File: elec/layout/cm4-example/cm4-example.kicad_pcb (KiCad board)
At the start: 4 copper layers, 109 parts, among them U10 10kΩ ±1% 62.5mW, U11 10kΩ ±1% 62.5mW, U13 1kΩ ±1% 62.5mW, U14 1kΩ ±1% 62.5mW, U15 100nF ±10% 16V X7R, U16 10kΩ ±1% 62.5mW, U17 10kΩ ±1% 62.5mW, U19 100nF ±10% 16V X7R, U2 1µF ±10% 25V X5R, U20 10kΩ ±1% 62.5mW, U21 10kΩ ±1% 62.5mW, U22 1kΩ ±1% 62.5mW, U23 1kΩ ±1% 62.5mW, U24 1µF ±10% 25V X5R, U26 1µF ±10% 25V X5R, U27 4.7µF ±10% 10V X5R, U28 10µF ±10% 10V X5R, U3 10kΩ ±1% 62.5mW, U31 1µF ±10% 25V X5R, U33 10pF ±5% 50V C0G, U34 10pF ±5% 50V C0G, U35 4.7µF ±10% 10V X5R, U36 10µF ±10% 10V X5R, U38 4.7nF ±10% 50V X7R, U39 60.4Ω ±1% 100mW, U4 10kΩ ±1% 62.5mW, U40 60.4Ω ±1% 100mW, U41 1µF ±10% 25V X5R, U42 1µF ±10% 25V X5R, U45 100nF ±10% 16V X7R, U46 2.2µF ±10% 25V X5R, U48 10kΩ ±1% 62.5mW, U49 10kΩ ±1% 62.5mW, U50 10kΩ ±1% 62.5mW, U51 10kΩ ±1% 62.5mW, U52 10kΩ ±1% 62.5mW, U53 10kΩ ±1% 62.5mW, U54 10kΩ ±1% 62.5mW, U55 10kΩ ±1% 62.5mW, U56 10kΩ ±1% 62.5mW, U57 10kΩ ±1% 62.5mW, U58 10kΩ ±1% 62.5mW, U59 10kΩ ±1% 62.5mW, U6 1kΩ ±1% 62.5mW, U60 10kΩ ±1% 62.5mW, U61 10kΩ ±1% 62.5mW, U62 10kΩ ±1% 62.5mW, U63 10kΩ ±1% 62.5mW, U64 10kΩ ±1% 62.5mW, U65 1kΩ ±1% 62.5mW, U66 1kΩ ±1% 62.5mW, U67 1µF ±10% 25V X5R, U69 1µF ±10% 25V X5R, U7 1kΩ ±1% 62.5mW, U70 470nF ±20% 16V X5R, U71 1kΩ ±1% 62.5mW, U72 1kΩ ±1% 62.5mW, U75 2.2µF ±20% 6.3V X5R, U76 10µF ±10% 25V X5R, U9 1µF ±10% 25V X5R

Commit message: initial routuing
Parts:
- moved U62 107.6 mm to (170.1, 94.9), turned to 90 degrees
- moved U45 107.4 mm to (173.1, 88.4), turned to 90 degrees
- moved U63 105.8 mm to (169.0, 94.9), turned to 90 degrees
- moved U46 104.9 mm to (171.8, 88.4), turned to 90 degrees
- moved U60 104.0 mm to (168.0, 94.9), turned to 90 degrees
- moved U61 102.3 mm to (166.9, 94.9), turned to 90 degrees
- moved U58 100.5 mm to (165.9, 94.9), turned to 90 degrees
- moved U64 99.7 mm to (171.2, 82.5), turned to 90 degrees
- moved U59 98.7 mm to (164.8, 94.9), turned to 90 degrees
- moved U49 97.7 mm to (170.1, 82.5), turned to -90 degrees
- moved U56 97.0 mm to (163.8, 94.9), turned to 90 degrees
- moved U47 95.8 mm to (166.7, 88.6), turned to 180 degrees
- moved U48 95.6 mm to (169.0, 82.5), turned to -90 degrees
- moved U57 95.3 mm to (162.8, 94.9), turned to 90 degrees
- moved U51 93.6 mm to (168.0, 82.5), turned to -90 degrees
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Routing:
- net cs: track 0.00 -> 54.9 mm, vias 0 -> 2
- net sck: track 0.00 -> 50.9 mm
- net mosi: track 0.00 -> 50.5 mm
- net miso: track 0.00 -> 45.7 mm
- net hv-3: track 47.3 -> 74.6 mm, vias 0 -> 9
- net gnd: track 66.3 -> 91.7 mm
- net io-1: track 0.00 -> 13.9 mm
- net VSINK_VCC: track 0.00 -> 13.3 mm
- net CANL: track 4.55 -> 17.4 mm
- net hv-1: track 16.7 -> 28.7 mm, vias 0 -> 2
- net VCC_5V: track 12.4 -> 22.5 mm
- net CANH: track 7.34 -> 15.2 mm
- net gnd-2: track 45.0 -> 52.2 mm
- added copper zone on F.Cu, net cathode-1
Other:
- board outline added: 100 x 100 mm

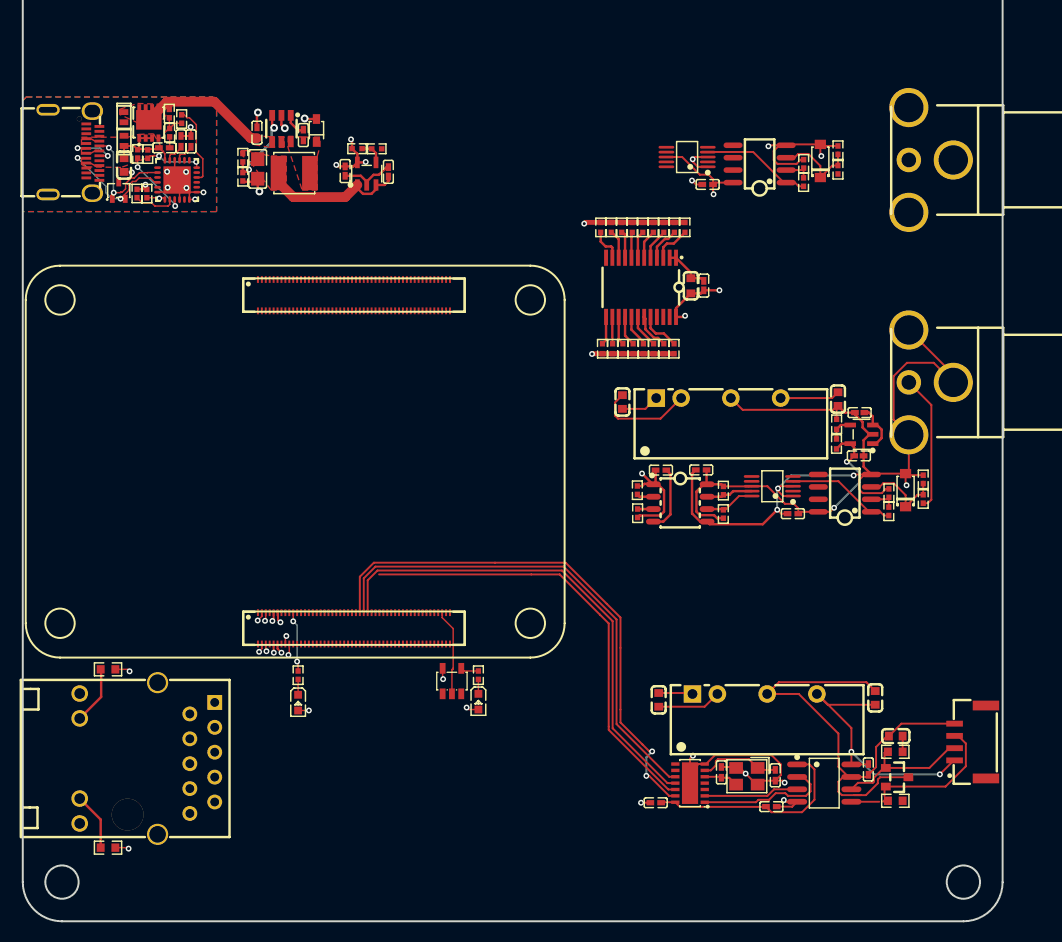
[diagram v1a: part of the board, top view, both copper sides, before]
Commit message: fixed SPI pinout
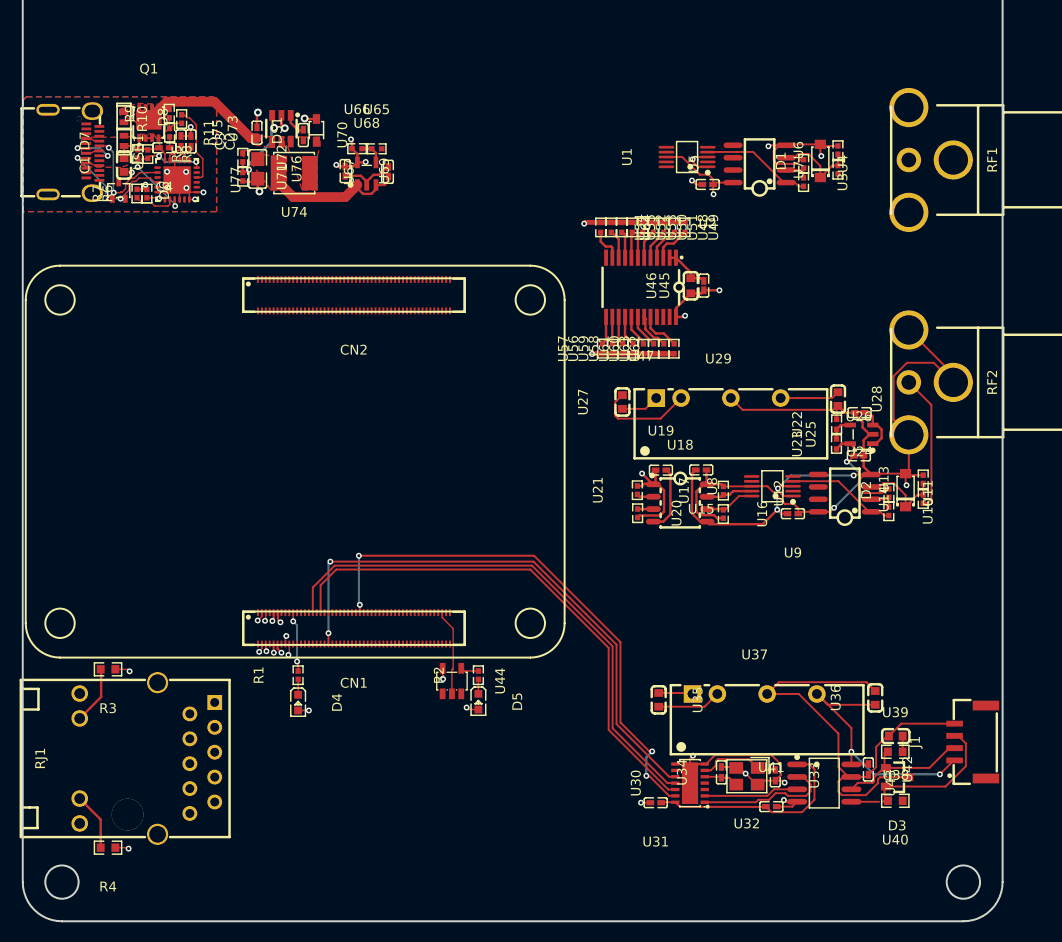
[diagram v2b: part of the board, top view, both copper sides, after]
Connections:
- net ADJ_NC renamed regulator_3v3-out
- net FB renamed regulator_5v-out
- net controller-line-2 renamed controller.cm4-pins[38]
- net out renamed analog_in_2.regulator_3v3_isolated-out
- net pins[38] renamed controller.cm4.hdi_b-pins[38]
- CN1 pad 15: controller-line-3 -> mosi
- CN1 pad 17: controller-line-1 -> miso
- CN1 pad 20: controller.cm4-line -> controller.cm4-line-1
- CN1 pad 22: controller.cm4-line-1 -> controller.cm4-line-3
- CN1 pad 28: sck -> pins[55]
- CN1 pad 29: mosi -> controller.cm4-line-2
- CN1 pad 78: controller.cm4-pins[44]-1 -> controller.cm4-pins[44]
- CN1 pad 80: controller.cm4-line-2 -> controller.cm4-line
- CN1 pad 82: controller-line -> sck
- CN2 pad 78: controller.cm4-pins[44] -> controller.cm4-pins[44]-1
- D1 pad 1: cathode -> cathode-2
- D2 pad 1: cathode-2 -> cathode-1
- D2 pad 2: gnd -> gnd-1
- D3 pad 3: gnd-2 -> gnd
- DS1 pad 1: cathode-1 -> cathode
- J1 pad 1: hv-1 -> hv-2
- J1 pad 4: gnd-2 -> gnd
- RF2 pad 2: gnd -> gnd-1
- RF2 pad 3: gnd -> gnd-1
- RF2 pad 4: gnd -> gnd-1
- RJ1 pad P1: controller.rj45.connector-net-1 -> controller.rj45.connector-net
- RJ1 pad P10: controller.rj45.connector-net -> controller.rj45.connector-net-1
- RJ1 pad SHIELD0: gnd-1 -> gnd-2
- RJ1 pad SHIELD1: gnd-1 -> gnd-2
- U1 pad 10: line -> line-3
- U1 pad 4: output -> output-1
- U1 pad 8: hv-3 -> hv
- U1 pad 9: line-2 -> line-1
- U10 pad 2: output-1 -> output
- U11 pad 1: gnd -> gnd-1
- U12 pad 1: output-1 -> output
- U12 pad 3: cathode-2 -> cathode-1
- U12 pad 4: gnd -> gnd-1
- U12 pad 8: hv-2 -> hv-3
- U13 pad 1: cathode-2 -> cathode-1
- U13 pad 2: gnd -> gnd-1
- U14 pad 2: cathode-2 -> cathode-1
- U15 pad 1: hv-2 -> hv-3
- U15 pad 2: gnd -> gnd-1
- U16 pad 2: hv-2 -> hv-3
- U17 pad 2: hv-2 -> hv-3
- U18 pad 1: hv-3 -> hv
- U18 pad 2: line-3 -> line
- U18 pad 3: line-1 -> line-2
- U18 pad 5: gnd -> gnd-1
- U18 pad 8: hv-2 -> hv-3
- U19 pad 1: hv-3 -> hv
- U2 pad 1: hv-3 -> hv
- U20 pad 1: line-1 -> line-2
- U20 pad 2: hv-3 -> hv
- U21 pad 1: line-3 -> line
- U21 pad 2: hv-3 -> hv
- U22 pad 2: gnd -> gnd-1
- U23 pad 1: hv-2 -> hv-3
- U24 pad 1: hv -> hv-1
- U24 pad 2: gnd -> gnd-1
- U25 pad 1: hv -> hv-1
- U25 pad 2: gnd -> gnd-1
- U25 pad 3: hv -> hv-1
- U25 pad 5: hv-2 -> hv-3
- U26 pad 1: hv-2 -> hv-3
- U26 pad 2: gnd -> gnd-1
- U28 pad 1: hv -> hv-1
- U28 pad 2: gnd -> gnd-1
- U29 pad 4: gnd -> gnd-1
- U29 pad 6: hv -> hv-1
- U3 pad 2: output -> output-1
- U30 pad 14: hv-3 -> hv
- U30 pad 4: can_interface.controller-io -> can_interface.controller-io-2
- U30 pad 8: can_interface.controller-io-1 -> can_interface.controller-io
- U30 pad 9: can_interface.controller-io-2 -> can_interface.controller-io-1
- U31 pad 1: hv-3 -> hv
- U36 pad 1: hv-1 -> hv-2
- U36 pad 2: gnd-2 -> gnd
- U37 pad 4: gnd-2 -> gnd
- U37 pad 6: hv-1 -> hv-2
- U38 pad 2: gnd-2 -> gnd
- U41 pad 1: hv-3 -> hv
- U42 pad 1: hv-1 -> hv-2
- U42 pad 2: gnd-2 -> gnd
- U43 pad 1: hv-3 -> hv
- U43 pad 7: gnd-2 -> gnd
- U43 pad 8: hv-1 -> hv-2
- U45 pad 1: hv-3 -> hv
- U46 pad 1: hv-3 -> hv
- U47 pad 10: i2c_multiplexer-line-1 -> i2c_multiplexer-line-8
- U47 pad 11: i2c_multiplexer-line-8 -> i2c_multiplexer-line-4
- U47 pad 13: line-3 -> line
- U47 pad 14: line-1 -> line-2
- U47 pad 15: i2c_multiplexer-line-4 -> i2c_multiplexer-line-3
- U47 pad 16: i2c_multiplexer-line-6 -> i2c_multiplexer-line-11
- U47 pad 18: i2c_multiplexer-line-5 -> i2c_multiplexer-line
- U47 pad 19: i2c_multiplexer-line-3 -> i2c_multiplexer-line-1
- U47 pad 20: i2c_multiplexer-line-7 -> i2c_multiplexer-line-10
- U47 pad 24: hv-3 -> hv
- U47 pad 4: line-2 -> line-1
- U47 pad 5: line -> line-3
- U47 pad 6: i2c_multiplexer-line-9 -> i2c_multiplexer-line-5
- U47 pad 7: i2c_multiplexer-line-10 -> i2c_multiplexer-line-6
- U47 pad 8: i2c_multiplexer-line -> i2c_multiplexer-line-9
- U47 pad 9: i2c_multiplexer-line-11 -> i2c_multiplexer-line-7
- U48 pad 1: hv-3 -> hv
- U48 pad 2: line -> line-3
- U49 pad 1: hv-3 -> hv
- U49 pad 2: line-2 -> line-1
- U5 pad 1: output -> output-1
- U5 pad 3: cathode -> cathode-2
- U5 pad 8: hv-3 -> hv
- U50 pad 1: hv-3 -> hv
- U50 pad 2: i2c_multiplexer-line-10 -> i2c_multiplexer-line-6
- U51 pad 1: hv-3 -> hv
- U51 pad 2: i2c_multiplexer-line-9 -> i2c_multiplexer-line-5
- U52 pad 1: hv-3 -> hv
- U52 pad 2: i2c_multiplexer-line-11 -> i2c_multiplexer-line-7
- U53 pad 1: hv-3 -> hv
- U53 pad 2: i2c_multiplexer-line -> i2c_multiplexer-line-9
- U54 pad 1: hv-3 -> hv
- U54 pad 2: i2c_multiplexer-line-8 -> i2c_multiplexer-line-4
- U55 pad 1: hv-3 -> hv
- U55 pad 2: i2c_multiplexer-line-1 -> i2c_multiplexer-line-8
- U56 pad 1: hv-3 -> hv
- U56 pad 2: line-1 -> line-2
- U57 pad 1: hv-3 -> hv
- U57 pad 2: line-3 -> line
- U58 pad 1: hv-3 -> hv
- U58 pad 2: i2c_multiplexer-line-6 -> i2c_multiplexer-line-11
- U59 pad 1: hv-3 -> hv
- U59 pad 2: i2c_multiplexer-line-4 -> i2c_multiplexer-line-3
- U6 pad 1: cathode -> cathode-2
- U60 pad 1: hv-3 -> hv
- U60 pad 2: i2c_multiplexer-line-5 -> i2c_multiplexer-line
- U61 pad 1: hv-3 -> hv
- U62 pad 1: hv-3 -> hv
- U62 pad 2: i2c_multiplexer-line-7 -> i2c_multiplexer-line-10
- U63 pad 1: hv-3 -> hv
- U63 pad 2: i2c_multiplexer-line-3 -> i2c_multiplexer-line-1
- U64 pad 2: hv-3 -> hv
- U66 pad 1: hv-3 -> hv
- U68 pad 5: hv-3 -> hv
- U69 pad 1: hv-3 -> hv
- U7 pad 2: cathode -> cathode-2
- U70 pad 2: cathode-1 -> cathode
- U73 pad 6: cathode-1 -> cathode
- U74 pad 1: cathode-1 -> cathode
- U77 pad 1: usb_pd.pd_controller.pd_controller-line-1 -> usb_pd.pd_controller.pd_controller-line
- U77 pad 5: usb_pd.pd_controller.pd_controller-line -> usb_pd.pd_controller.pd_controller-line-1
- U8 pad 1: gnd -> gnd-1
- U8 pad 3: gnd -> gnd-1
- U8 pad 4: output-1 -> output
- U8 pad 8: hv-2 -> hv-3
- U9 pad 1: hv-2 -> hv-3
- U9 pad 2: gnd -> gnd-1
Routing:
- net gnd-1: track 0.00 -> 91.7 mm, vias 0 -> 4
- net hv: track 11.1 -> 74.6 mm, vias 0 -> 9
- net gnd-2: track 52.2 -> 0.00 mm
- net hv-3: track 74.6 -> 33.2 mm, vias 9 -> 2
- net gnd: track 91.7 -> 52.2 mm, vias 4 -> 0
- net hv-1: track 28.7 -> 11.1 mm, vias 2 -> 0
- net cathode: track 8.99 -> 0.00 mm
- net cathode-1: track 0.00 -> 8.99 mm
- net miso: track 45.7 -> 53.9 mm
- net sck: track 50.9 -> 57.5 mm, vias 0 -> 2
- net hv-2: track 33.2 -> 28.7 mm
- net mosi: track 50.5 -> 54.6 mm
- net line-3: track 4.62 -> 3.13 mm
- net line: track 3.13 -> 4.62 mm
- net i2c_multiplexer-line-7: track 4.21 -> 2.78 mm
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- added copper zone on B.Cu, net (none)
- added copper zone on F.Cu, net (none)
- added copper zone on F.Cu, net cathode
- removed copper zone on B.Cu, net GND
- removed copper zone on F.Cu, net GND
- removed copper zone on F.Cu, net cathode-1

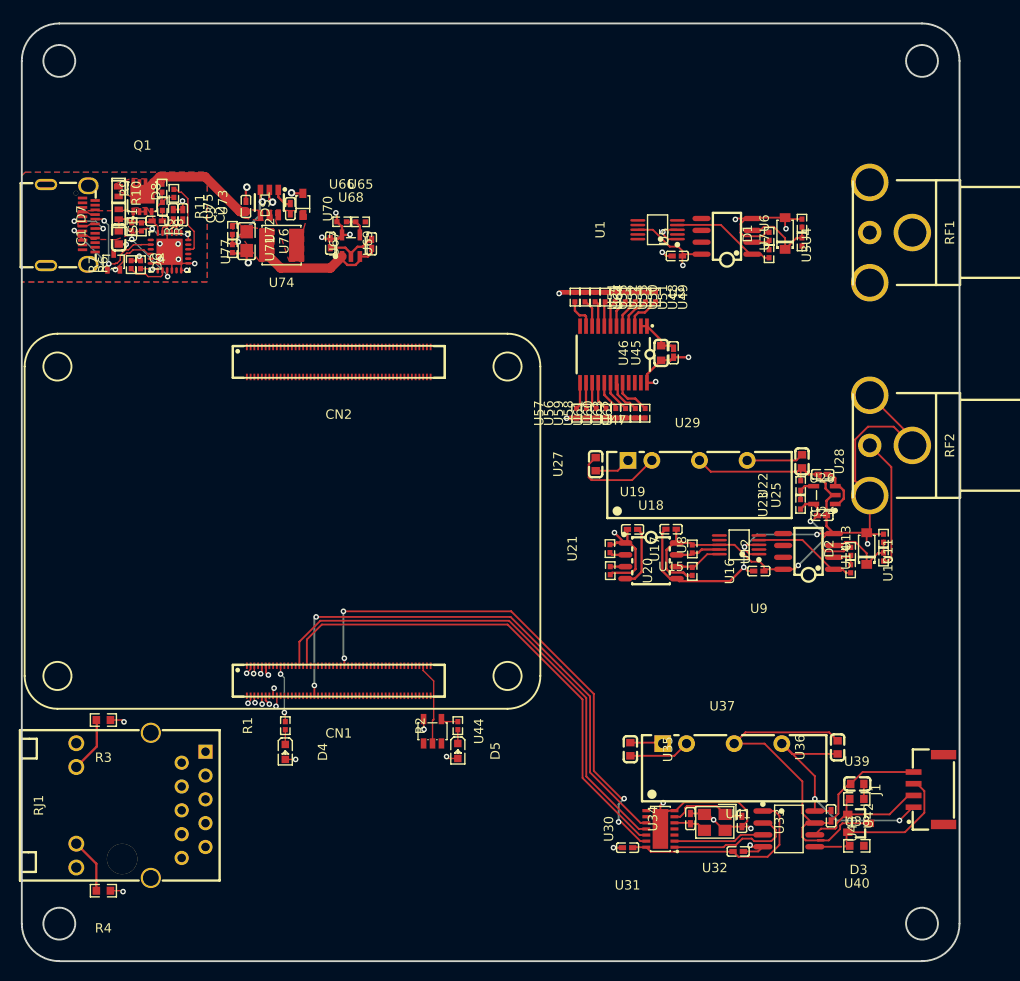
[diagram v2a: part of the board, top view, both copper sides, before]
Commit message: zone islanding issue
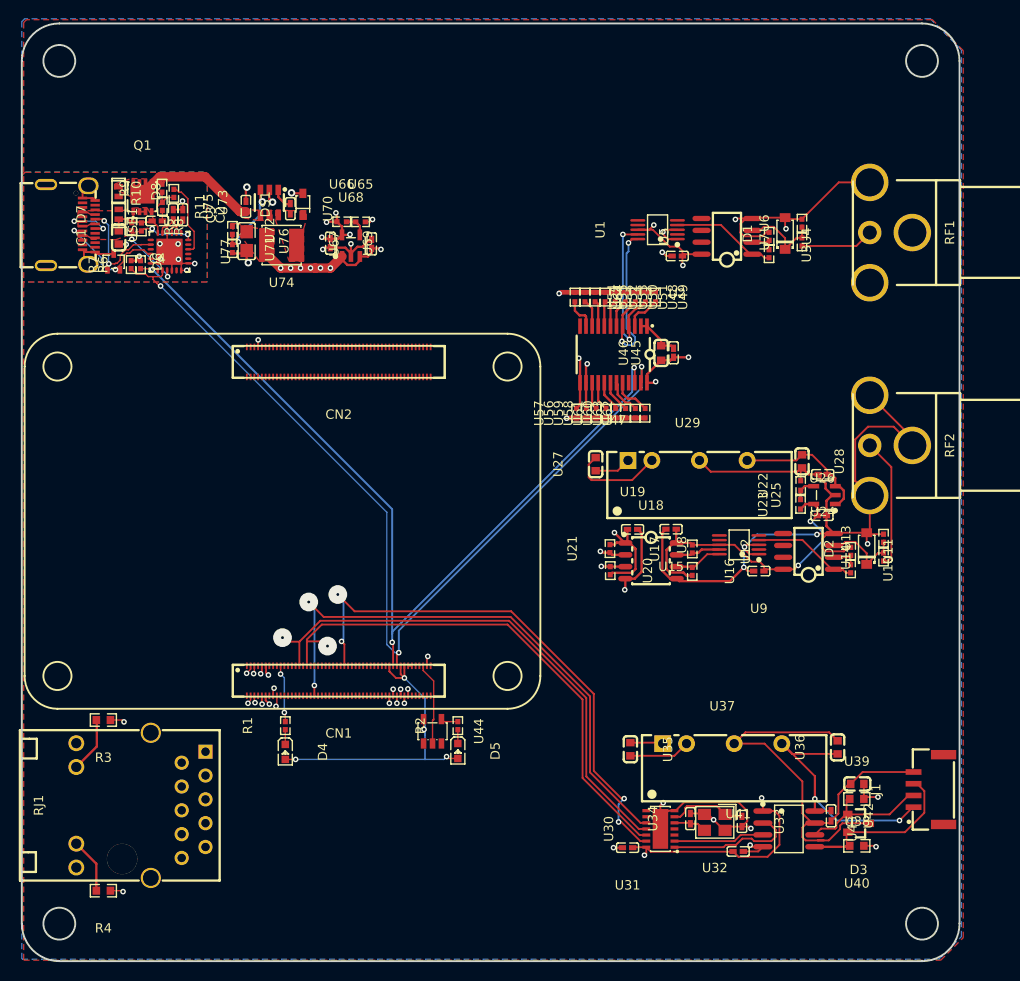
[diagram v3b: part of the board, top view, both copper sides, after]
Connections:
- net RESET_ renamed i2c_multiplexer-io
- net analog_in_2.regulator_3v3_isolated-out renamed ADJ_NC
- net can_interface.controller-io-1 renamed INT0h_GPIO0_XSTBY
- net can_interface.controller-io-2 renamed INTh
- net can_interface.controller-io-3 renamed CLKO_SOF
- CN1 pad 20: controller.cm4-line-1 -> controller.cm4-line-2
- CN1 pad 22: controller.cm4-line-3 -> controller.cm4-line
- CN1 pad 29: controller.cm4-line-2 -> controller.cm4-line-3
- CN1 pad 78: controller.cm4-pins[44] -> controller.cm4-pins[44]-1
- CN1 pad 80: controller.cm4-line -> controller.cm4-line-1
- CN2 pad 78: controller.cm4-pins[44]-1 -> controller.cm4-pins[44]
- D2 pad 1: cathode-1 -> cathode
- D2 pad 2: gnd-1 -> gnd
- D3 pad 3: gnd -> gnd-2
- D4 pad 1: controller.cm4-cathode-1 -> controller.cm4-cathode
- D5 pad 1: controller.cm4-cathode -> controller.cm4-cathode-1
- DS1 pad 1: cathode -> cathode-1
- J1 pad 4: gnd -> gnd-2
- R1 pad 1: controller.cm4-cathode-1 -> controller.cm4-cathode
- R2 pad 1: controller.cm4-cathode -> controller.cm4-cathode-1
- R3 pad 1: controller.rj45-hv -> VCC_3V3
- R3 pad 2: controller.rj45-anode-1 -> controller.rj45-anode
- R4 pad 1: controller.rj45-hv -> VCC_3V3
- R4 pad 2: controller.rj45-anode -> controller.rj45-anode-1
- RF2 pad 2: gnd-1 -> gnd
- RF2 pad 3: gnd-1 -> gnd
- RF2 pad 4: gnd-1 -> gnd
- RJ1 pad 12: controller.rj45-anode-1 -> controller.rj45-anode
- RJ1 pad 13: controller.rj45-anode -> controller.rj45-anode-1
- RJ1 pad P1: controller.rj45.connector-net -> controller.rj45.connector-net-1
- RJ1 pad P10: controller.rj45.connector-net-1 -> controller.rj45.connector-net
- RJ1 pad SHIELD0: gnd-2 -> gnd-1
- RJ1 pad SHIELD1: gnd-2 -> gnd-1
- U1 pad 10: line-3 -> line-2
- U1 pad 8: hv -> hv-1
- U1 pad 9: line-1 -> line-3
- U11 pad 1: gnd-1 -> gnd
- U12 pad 3: cathode-1 -> cathode
- U12 pad 4: gnd-1 -> gnd
- U13 pad 1: cathode-1 -> cathode
- U13 pad 2: gnd-1 -> gnd
- U14 pad 2: cathode-1 -> cathode
- U15 pad 2: gnd-1 -> gnd
- U18 pad 1: hv -> hv-1
- U18 pad 2: line -> line-1
- U18 pad 3: line-2 -> line
- U18 pad 5: gnd-1 -> gnd
- U19 pad 1: hv -> hv-1
- U2 pad 1: hv -> hv-1
- U20 pad 1: line-2 -> line
- U20 pad 2: hv -> hv-1
- U21 pad 1: line -> line-1
- U21 pad 2: hv -> hv-1
- U22 pad 2: gnd-1 -> gnd
- U24 pad 1: hv-1 -> hv
- U24 pad 2: gnd-1 -> gnd
- U25 pad 1: hv-1 -> hv
- U25 pad 2: gnd-1 -> gnd
- U25 pad 3: hv-1 -> hv
- U26 pad 2: gnd-1 -> gnd
- U28 pad 1: hv-1 -> hv
- U28 pad 2: gnd-1 -> gnd
- U29 pad 4: gnd-1 -> gnd
- U29 pad 6: hv-1 -> hv
- U30 pad 14: hv -> hv-1
- U31 pad 1: hv -> hv-1
- U36 pad 2: gnd -> gnd-2
- U37 pad 4: gnd -> gnd-2
- U38 pad 2: gnd -> gnd-2
- U41 pad 1: hv -> hv-1
- U42 pad 2: gnd -> gnd-2
- U43 pad 1: hv -> hv-1
- U43 pad 7: gnd -> gnd-2
- U45 pad 1: hv -> hv-1
- U46 pad 1: hv -> hv-1
- U47 pad 10: i2c_multiplexer-line-8 -> i2c_multiplexer-line-7
- U47 pad 11: i2c_multiplexer-line-4 -> i2c_multiplexer-line-10
- U47 pad 13: line -> line-1
- U47 pad 14: line-2 -> line
- U47 pad 15: i2c_multiplexer-line-3 -> i2c_multiplexer-line-5
- U47 pad 16: i2c_multiplexer-line-11 -> i2c_multiplexer-line-9
- U47 pad 17: i2c_multiplexer-line-2 -> i2c_multiplexer-line-1
- U47 pad 18: i2c_multiplexer-line -> i2c_multiplexer-line-2
- U47 pad 19: i2c_multiplexer-line-1 -> i2c_multiplexer-line-11
- U47 pad 20: i2c_multiplexer-line-10 -> i2c_multiplexer-line
- U47 pad 24: hv -> hv-1
- U47 pad 4: line-1 -> line-3
- U47 pad 5: line-3 -> line-2
- U47 pad 6: i2c_multiplexer-line-5 -> i2c_multiplexer-line-3
- U47 pad 8: i2c_multiplexer-line-9 -> i2c_multiplexer-line-8
- U47 pad 9: i2c_multiplexer-line-7 -> i2c_multiplexer-line-4
- U48 pad 1: hv -> hv-1
- U48 pad 2: line-3 -> line-2
- U49 pad 1: hv -> hv-1
- U49 pad 2: line-1 -> line-3
- U5 pad 8: hv -> hv-1
- U50 pad 1: hv -> hv-1
- U51 pad 1: hv -> hv-1
- U51 pad 2: i2c_multiplexer-line-5 -> i2c_multiplexer-line-3
- U52 pad 1: hv -> hv-1
- U52 pad 2: i2c_multiplexer-line-7 -> i2c_multiplexer-line-4
- U53 pad 1: hv -> hv-1
- U53 pad 2: i2c_multiplexer-line-9 -> i2c_multiplexer-line-8
- U54 pad 1: hv -> hv-1
- U54 pad 2: i2c_multiplexer-line-4 -> i2c_multiplexer-line-10
- U55 pad 1: hv -> hv-1
- U55 pad 2: i2c_multiplexer-line-8 -> i2c_multiplexer-line-7
- U56 pad 1: hv -> hv-1
- U56 pad 2: line-2 -> line
- U57 pad 1: hv -> hv-1
- U57 pad 2: line -> line-1
- U58 pad 1: hv -> hv-1
- U58 pad 2: i2c_multiplexer-line-11 -> i2c_multiplexer-line-9
- U59 pad 1: hv -> hv-1
- U59 pad 2: i2c_multiplexer-line-3 -> i2c_multiplexer-line-5
- U60 pad 1: hv -> hv-1
- U60 pad 2: i2c_multiplexer-line -> i2c_multiplexer-line-2
- U61 pad 1: hv -> hv-1
- U61 pad 2: i2c_multiplexer-line-2 -> i2c_multiplexer-line-1
- U62 pad 1: hv -> hv-1
- U62 pad 2: i2c_multiplexer-line-10 -> i2c_multiplexer-line
- U63 pad 1: hv -> hv-1
- U63 pad 2: i2c_multiplexer-line-1 -> i2c_multiplexer-line-11
- U64 pad 2: hv -> hv-1
- U66 pad 1: hv -> hv-1
- U68 pad 5: hv -> hv-1
- U69 pad 1: hv -> hv-1
- U70 pad 2: cathode -> cathode-1
- U73 pad 6: cathode -> cathode-1
- U74 pad 1: cathode -> cathode-1
- U8 pad 1: gnd-1 -> gnd
- U8 pad 3: gnd-1 -> gnd
- U9 pad 2: gnd-1 -> gnd
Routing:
- net GND: track 103.9 -> 0.00 mm, vias 21 -> 0
- net SDA: track 4.26 -> 100.0 mm, vias 0 -> 3
- net (no net): track 0.00 -> 95.7 mm, vias 0 -> 22
- net SCL: track 2.17 -> 95.8 mm, vias 1 -> 3
- net VCC_3V3: track 3.50 -> 88.8 mm, vias 3 -> 6
- net gnd-1: track 91.7 -> 15.5 mm, vias 4 -> 0
- net hv-1: track 11.1 -> 80.0 mm, vias 0 -> 13
- net hv: track 74.6 -> 14.9 mm, vias 9 -> 0
- net gnd-2: track 0.00 -> 52.2 mm
- net gnd: track 52.2 -> 91.7 mm, vias 0 -> 4
- net analog_in_1.amplifier.opamp.footprint.pins[6].net-net: track 0.00 -> 34.8 mm, vias 0 -> 5
- net line-1: track 3.51 -> 32.0 mm, vias 0 -> 2
- net line: track 4.62 -> 30.9 mm, vias 0 -> 2
- net line-3: track 3.13 -> 18.0 mm, vias 0 -> 2
- net line-2: track 4.36 -> 18.6 mm, vias 0 -> 2
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- added copper zone on In2.Cu, net (none)
- added copper zone on B.Cu, net VCC_5V
- added copper zone on F.Cu, net cathode-1
- added copper zone on In1.Cu, net hv-1
- removed copper zone on F.Cu, net cathode
